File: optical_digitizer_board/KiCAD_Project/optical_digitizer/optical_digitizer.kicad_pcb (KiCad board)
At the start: 4 copper layers, 114.3 x 33 mm, 34 parts, among them J1 Female Input Connector, J2 Male Output Connector, U1 OPA350, U2 OPA350, U3 MCP3202

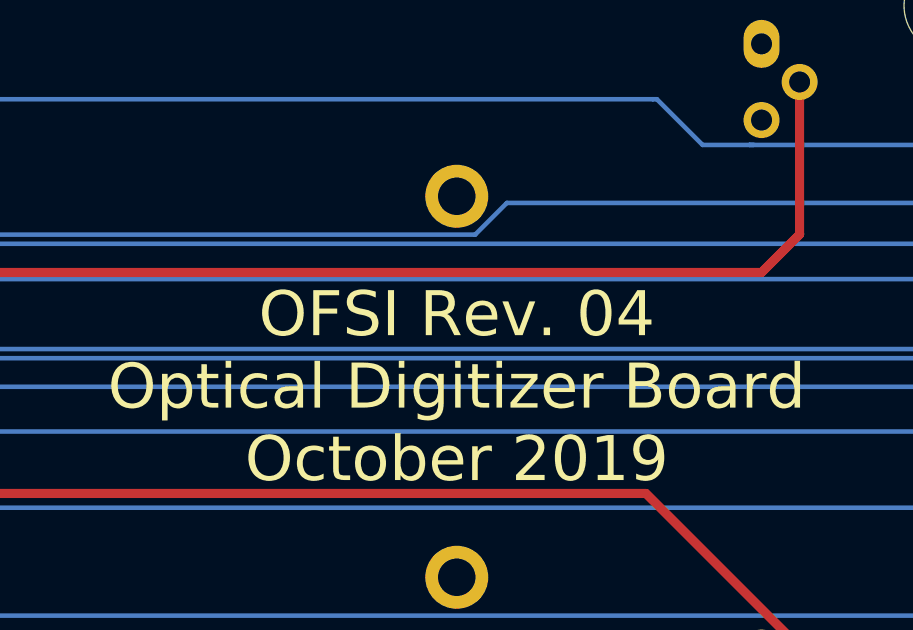
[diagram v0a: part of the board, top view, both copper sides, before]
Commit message: Change optical digitizer to OFMI
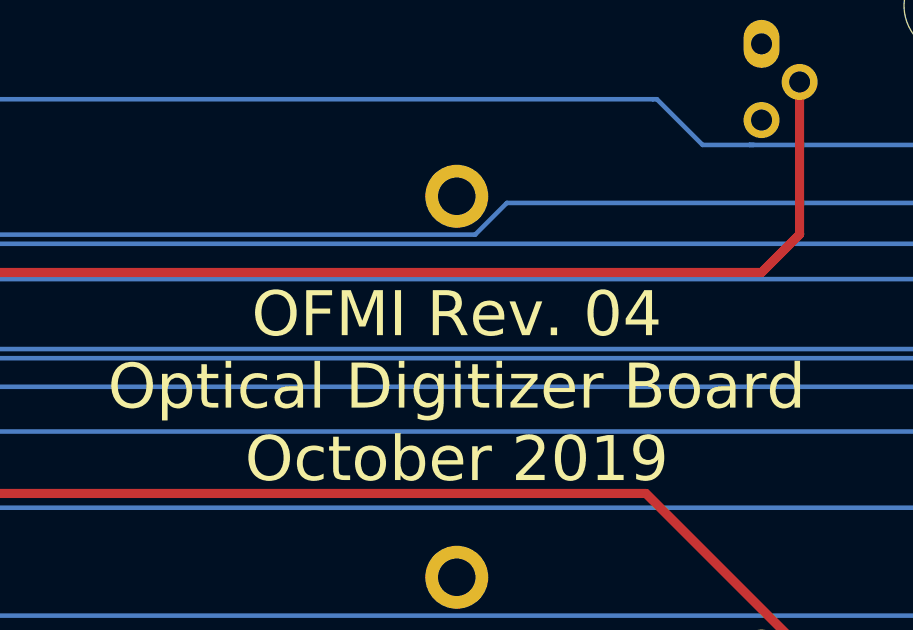
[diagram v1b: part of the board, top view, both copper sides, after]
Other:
- board text added: "OFMI Rev. 04 Optical Digitizer Board October 2019"
- board text removed: "OFSI Rev. 04 Optical Digitizer Board October 2019"
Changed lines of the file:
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@@
     (effects (font (size 0.762 0.762) (thickness 0.14986)) (justify mirror))
   )
-  (gr_text "OFSI Rev. 04\nOptical Digitizer Board\nOctober 2019" (at 154.94 135.89) (layer F.SilkS)
+  (gr_text "OFMI Rev. 04\nOptical Digitizer Board\nOctober 2019" (at 154.94 135.89) (layer F.SilkS)
     (effects (font (size 1.5 1.5) (thickness 0.3)))
   )

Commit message: Make changes for Rev 4.1
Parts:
- added R1: 10k, Resistor_SMD:R_0603_1608Metric, F.Cu at (119.1, 123.3)
- added R2: 10k, Resistor_SMD:R_0603_1608Metric, F.Cu at (119.1, 121.7)
- added R3: 10k, Resistor_SMD:R_0603_1608Metric, F.Cu at (119.6, 149.6)
- added R4: 10k, Resistor_SMD:R_0603_1608Metric, F.Cu at (119.6, 151.4)
- U1, U2: value OPA350 -> LM358AP; footprint Housings_DIP:DIP-8_W7.62mm -> Package_DIP:DIP-8_W7.62mm_LongPads
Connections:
- net CS1 renamed /MISO1
- net CS2 renamed /MISO2
- net CS3 renamed /MISO3
- net CS4 renamed /MISO4
- net CS5 renamed /MISO5
- net CS6 renamed /MISO6
- net CS7 renamed /MISO7
- net CS8 renamed /MISO8
- net CS9 renamed /MISO9
- net MOSI renamed /MOSI
- net SCLK renamed /SCLK
- J1 pad 15: MISO -> /CS
- J1 pad 3: +12V -> (no net)
- J1 pad 5: -12V -> (no net)
- J2 pad 15: MISO -> /CS
- J2 pad 3: +12V -> (no net)
- J2 pad 5: -12V -> (no net)
- JP1 pad 1: CS -> /MISO
- JP2 pad 1: CS -> /MISO
- JP3 pad 1: CS -> /MISO
- JP4 pad 1: CS -> /MISO
- JP5 pad 1: CS -> /MISO
- JP6 pad 1: CS -> /MISO
- JP7 pad 1: CS -> /MISO
- JP8 pad 1: CS -> /MISO
- JP9 pad 1: CS -> /MISO
- U1 pad 1: (no net) -> Net-(C5-Pad1)
- U1 pad 5: (no net) -> Net-(R1-Pad2)
- U1 pad 6: Net-(C5-Pad1) -> Net-(U1-Pad6)
- U1 pad 7: +5V -> Net-(U1-Pad6)
- U1 pad 8: (no net) -> +5V
- U2 pad 1: (no net) -> Net-(C6-Pad1)
- U2 pad 5: (no net) -> Net-(R3-Pad2)
- U2 pad 6: Net-(C6-Pad1) -> Net-(U2-Pad6)
- U2 pad 7: +5V -> Net-(U2-Pad6)
- U2 pad 8: (no net) -> +5V
- U3 pad 1: CS -> /CS
- U3 pad 6: MISO -> /MISO
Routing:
- net /MISO2: track 114.0 -> 65.3 mm
- net CS: track 36.5 -> 0.00 mm
- net CS2: track 0.00 -> 26.1 mm
- net MISO: track 116.5 -> 93.8 mm
- net +12V: track 100.6 -> 80.7 mm
- net Net-(C5-Pad1): track 46.3 -> 29.0 mm
- net Net-(C6-Pad1): track 38.3 -> 21.5 mm
- net Net-(D2-Pad2): track 44.9 -> 39.8 mm
- net Net-(D1-Pad2): track 49.0 -> 43.9 mm
- net -12V: track 101.3 -> 98.6 mm
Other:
- board text added: "5V"
- board text added: "CH0"
- board text added: "CH1"
- board text added: "LG 3-0000045"
- board text added: "MISO1"
- board text added: "MISO2"
- board text added: "MISO3"
- board text added: "MISO4"
- board text added: "MISO5"
- board text added: "MISO6"
- board text added: "MISO7"
- board text added: "MISO8"
- board text added: "MISO9"
- board text added: "OFMI Rev. 4.1 Optical Digitizer Board September 2020"
- board text removed: "+12V"
- board text removed: "-12V"
- board text removed: "CS1"
- board text removed: "CS2"
- board text removed: "CS3"
- board text removed: "CS4"
- board text removed: "CS5"
- board text removed: "CS6"
- board text removed: "CS7"
- board text removed: "CS8"
- board text removed: "CS9"
- board text removed: "LG3-0000014"
- board text removed: "OFMI Rev. 04 Optical Digitizer Board October 2019"

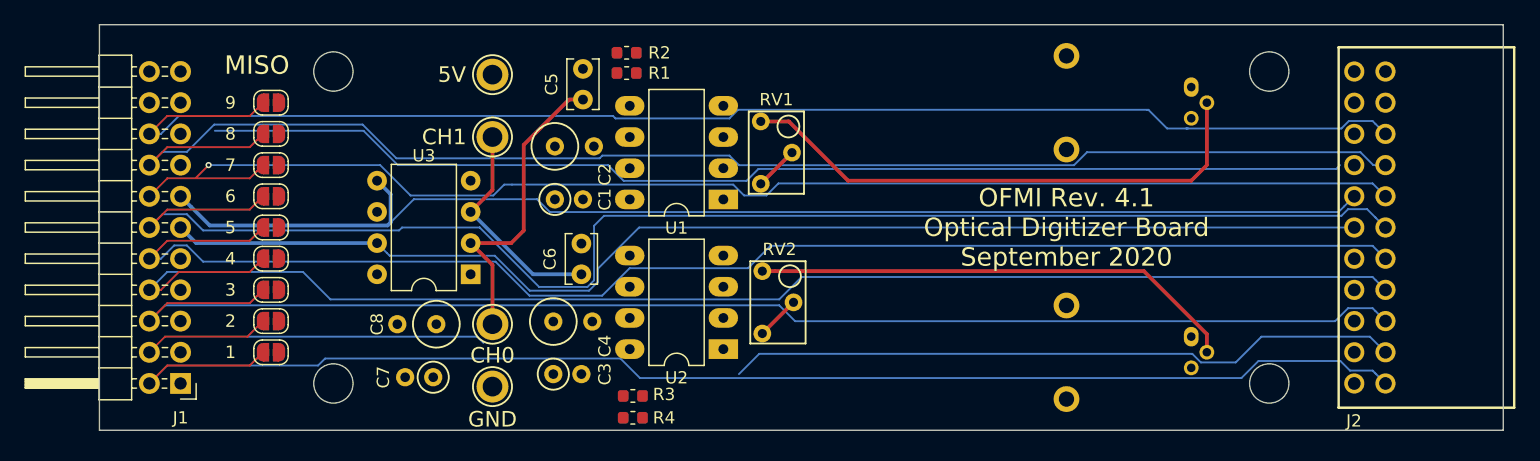
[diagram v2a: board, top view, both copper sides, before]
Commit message: Finalize optical digitizer
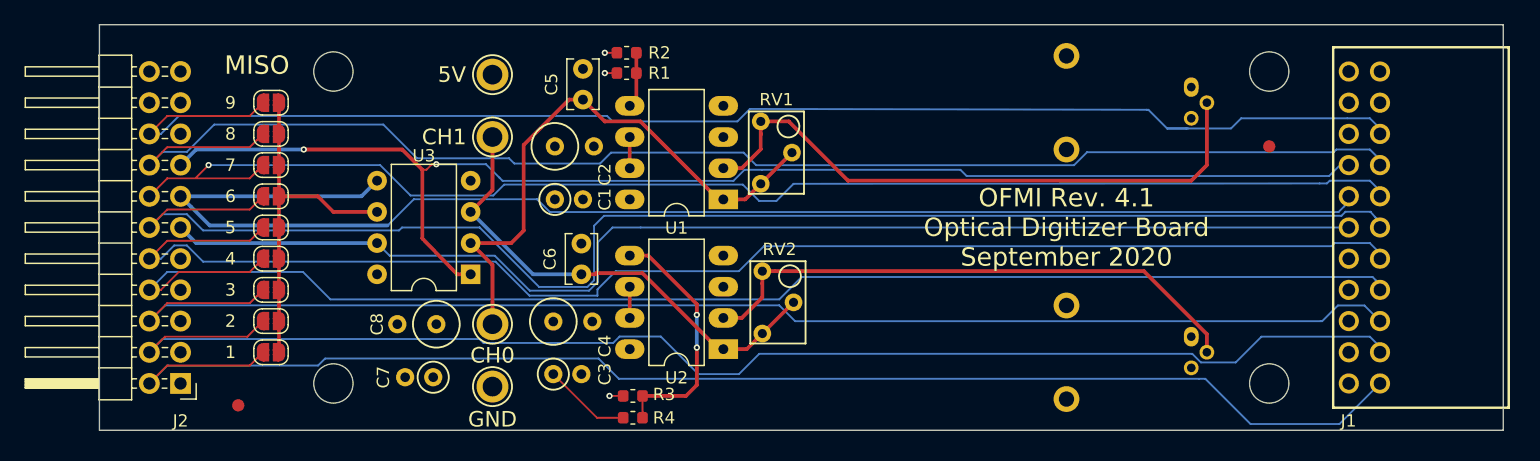
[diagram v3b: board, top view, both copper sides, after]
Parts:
- added FID1: Fiducial, Fiducial:Fiducial_1mm_Mask3mm, F.Cu at (87.5, 150.4)
- added FID2: Fiducial, Fiducial:Fiducial_1mm_Mask3mm, F.Cu at (171.4, 129.3)
- J1: renamed from J2; value Male Output Connector -> Female Input Connector
- J2: renamed from J1; value Female Input Connector -> Male Output Connector
- moved J1 0.44 mm to (186.2, 135.9)
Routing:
- net /CS: track 0.00 -> 109.2 mm, vias 0 -> 2
- net -12V: track 98.6 -> 0.00 mm
- net MISO: track 93.8 -> 0.00 mm
- net +12V: track 80.7 -> 0.00 mm
- net /MISO2: track 65.3 -> 115.4 mm
- net /MISO: track 0.00 -> 28.8 mm
- net CS2: track 26.1 -> 0.00 mm
- net Net-(R3-Pad2): track 0.00 -> 20.3 mm, vias 0 -> 2
- net Net-(C5-Pad1): track 29.0 -> 47.4 mm
- net Net-(C6-Pad1): track 21.5 -> 39.4 mm
- net /MOSI: track 102.6 -> 114.9 mm
- net GND: track 0.00 -> 8.15 mm, vias 0 -> 1
- net Net-(D2-Pad2): track 39.8 -> 45.8 mm
- net Net-(D1-Pad2): track 43.9 -> 49.9 mm
- net Net-(R1-Pad2): track 0.00 -> 4.54 mm
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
